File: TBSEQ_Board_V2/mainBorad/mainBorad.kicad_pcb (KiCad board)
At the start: 2 copper layers, 150 x 150 mm, 235 parts, among them IC11 AN6562, IC11_1 AN6562, IC12 4066, IC15 CA3080A, J13 Conn_01x01_Pin, J3 Conn_01x02_Pin, J4 Conn_01x02_Pin, J7 Conn_01x03_Pin, J8 Conn_01x02_Pin, J9 Conn_01x01_Pin, Q10 PNP, Q11 NPN, Q12 HN1C01FU-GR,LF_6P DIP, Q13 NPN, Q14 NPN, Q15 NPN, Q16 NPN, Q17 NPN, Q18 NPN, Q19 NPN, Q20 NPN, Q21 HN1C01FU-GR,LF_6P DIP, Q22 HN1C01FU-GR,LF_6P DIP, Q23 NPN, Q24 NPN, Q25 NPN, Q26 HN1C01FU-GR,LF_6P DIP, Q27 PNP, Q28 NJFET, Q29 NPN, Q30 NPN, Q31 PNP, Q32 NPN, Q35 NPN, Q36 PNP, Q37 NPN, Q38 PNP, Q39 NJFET, Q40 NPN, Q41 NPN, Q8 PNP, Q9 PNP

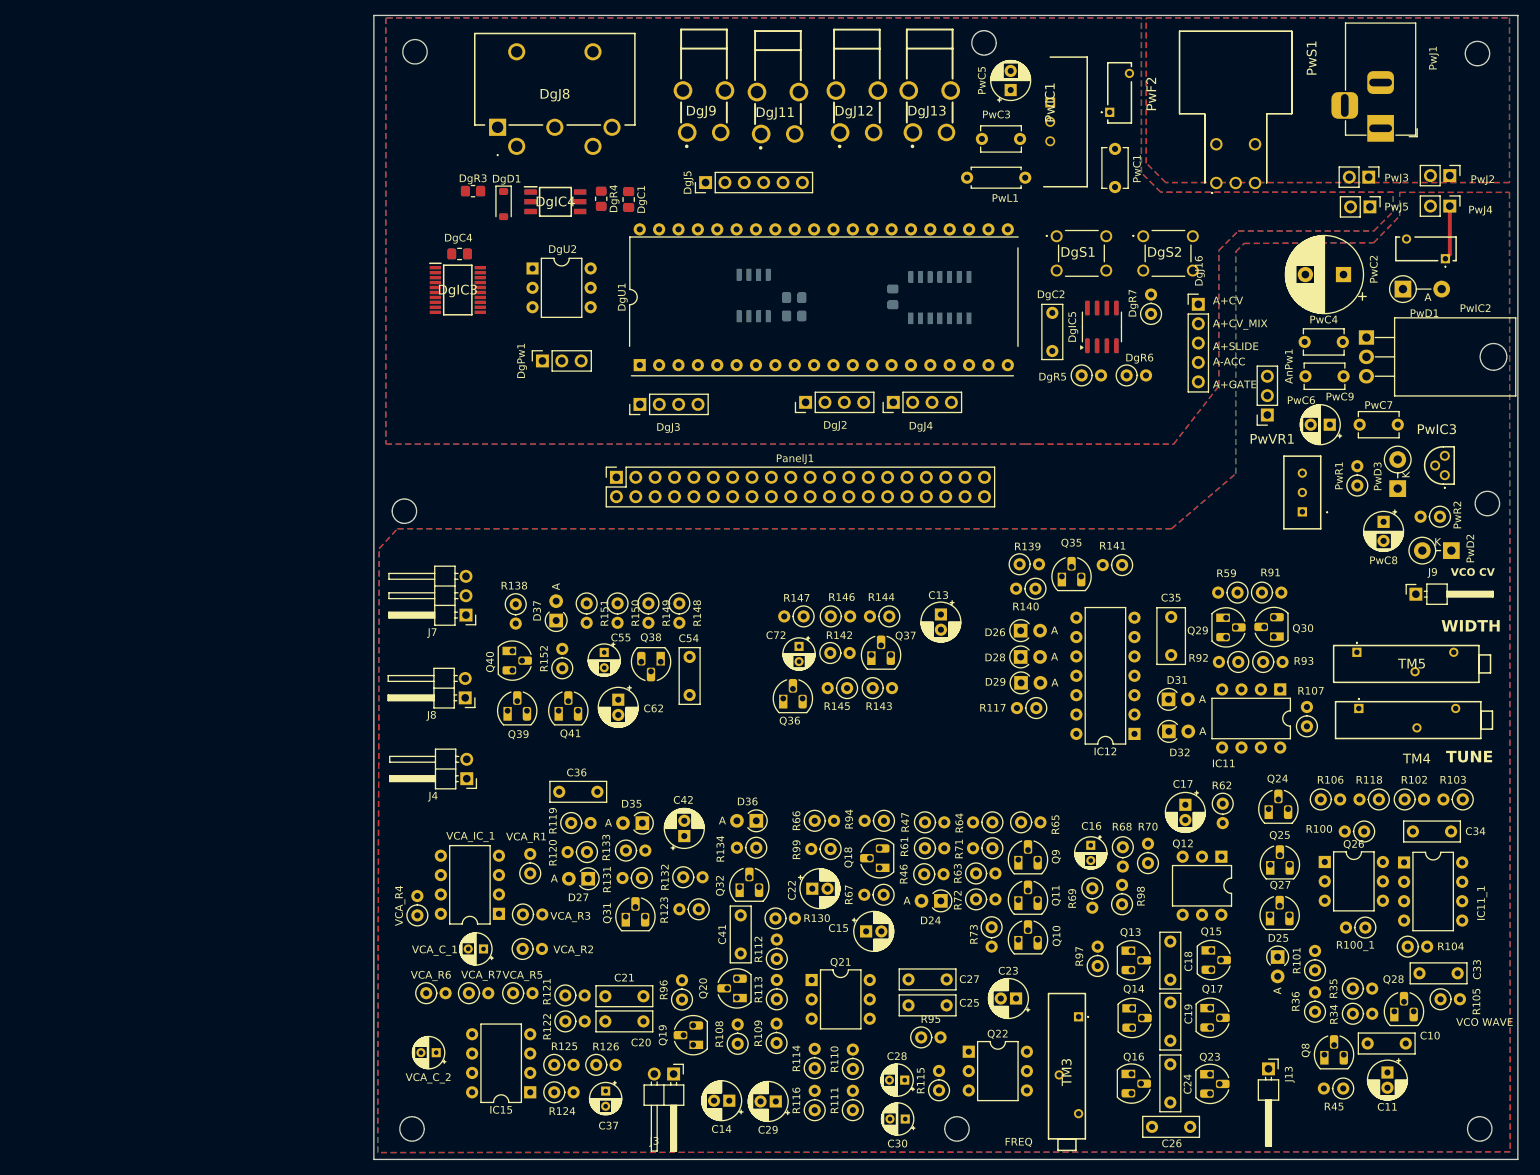
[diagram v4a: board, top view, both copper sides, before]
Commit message: mainborad
DRCチェック通過
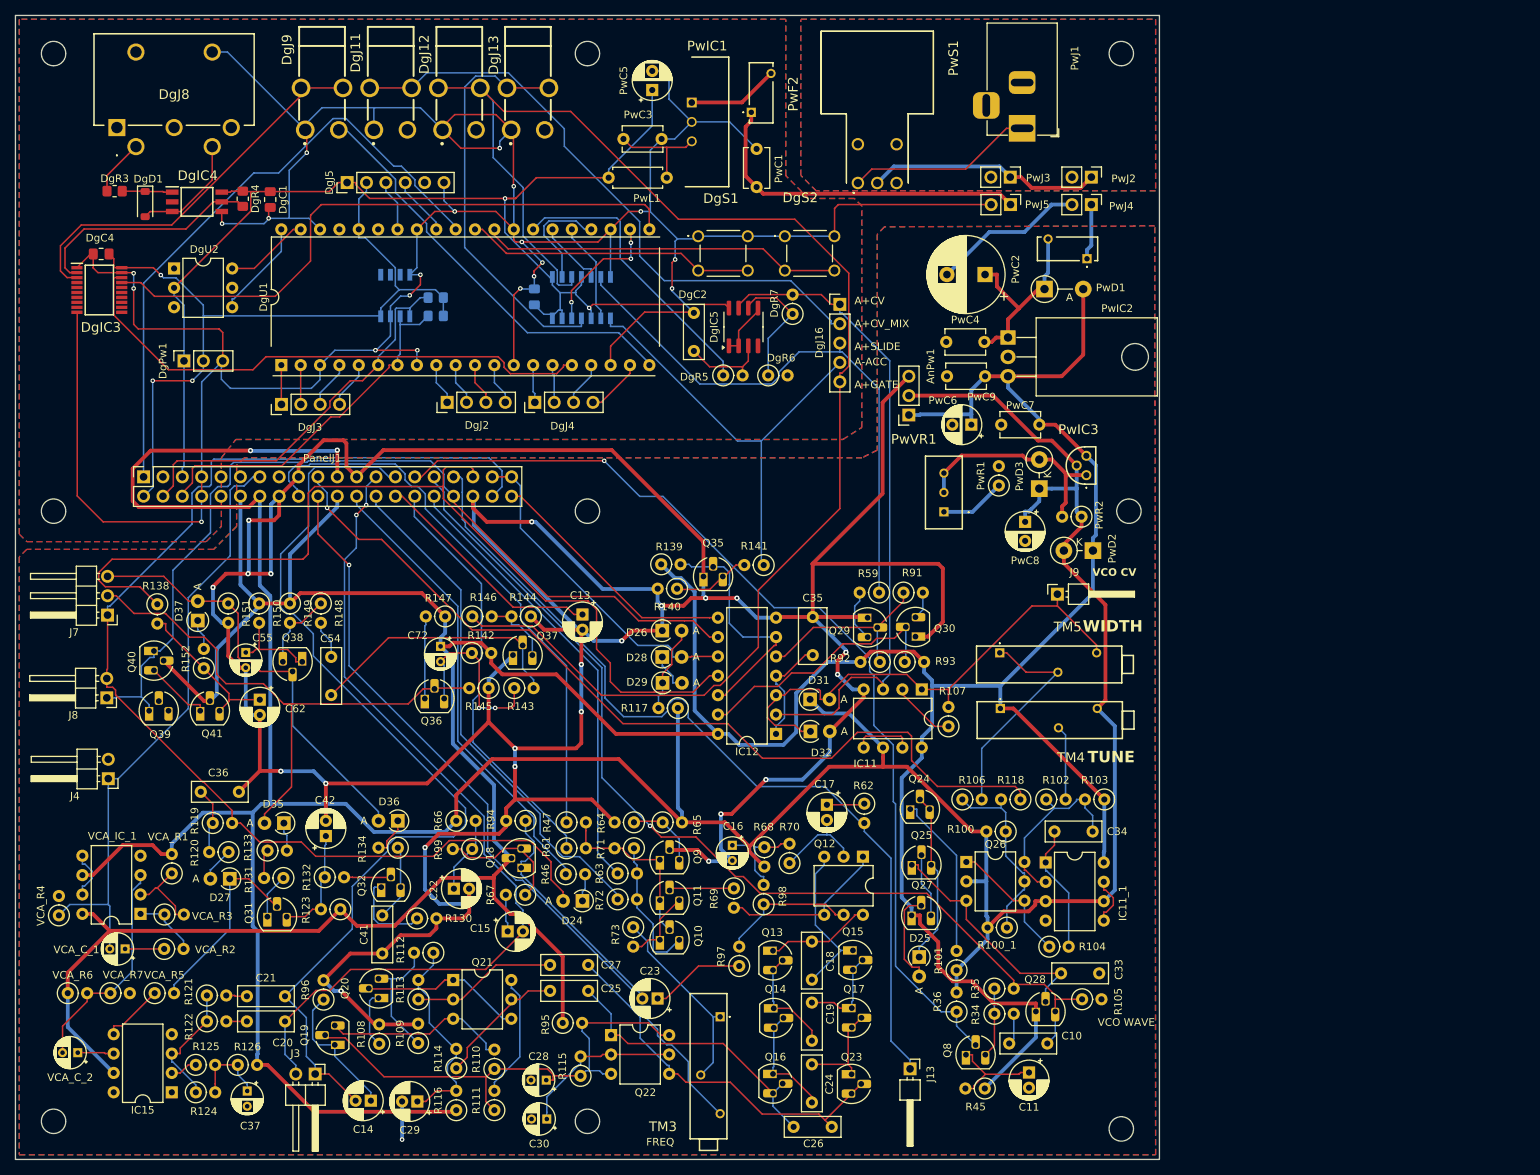
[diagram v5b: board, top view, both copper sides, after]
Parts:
- moved PanelJ1 62.0 mm to (36.8, 80.5)
- moved DgJ13 52.7 mm to (87.2, 24.0)
- moved DgJ12 52.1 mm to (78.2, 24.0)
- moved DgJ11 50.8 mm to (69.2, 24.0)
- moved DgJ9 50.1 mm to (60.2, 24.0)
- moved DgJ8 49.9 mm to (33.3, 34.7)
- moved PwJ5 47.1 mm to (150.5, 44.8)
- moved C25 47.0 mm to (95.1, 147.9)
- moved C27 47.0 mm to (95.1, 144.5)
- moved R115 47.0 mm to (94.1, 159.0)
- moved R95 47.0 mm to (91.8, 152.1)
- moved PwJ2 47.0 mm to (161.1, 41.2)
- moved PwJ4 47.0 mm to (161.1, 44.8)
- moved PwC6 47.0 mm to (145.3, 73.7)
- moved PwC5 47.0 mm to (103.5, 29.8)
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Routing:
- net GNDA: track 0.00 -> 567.8 mm, vias 0 -> 23
- net A+12V: track 0.00 -> 533.7 mm
- net A+5.333V: track 0.00 -> 475.0 mm, vias 0 -> 2
- net GNDD: track 0.00 -> 434.4 mm, vias 0 -> 20
- net A+GATE: track 0.00 -> 195.3 mm
- net D+5V: track 0.00 -> 162.4 mm, vias 0 -> 2
- net A+VCA-Reso_ACC: track 0.00 -> 155.7 mm
- net A+VCO_SAW: track 0.00 -> 131.0 mm, vias 0 -> 1
- net A+VCO_SQU: track 0.00 -> 128.9 mm, vias 0 -> 1
- net A_VR6_CCW: track 0.00 -> 125.9 mm
- net A+VCA_Signal: track 0.00 -> 125.6 mm
- net A+ENV.MOD: track 0.00 -> 118.7 mm
- net A_VR2_WIPER: track 0.00 -> 116.6 mm, vias 0 -> 1
- net A+VCO_WAVE: track 0.00 -> 116.6 mm
- net A+VCA_Resonance: track 0.00 -> 115.4 mm, vias 0 -> 2
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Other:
- outline, holes or cut-outs redrawn

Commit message: mainboard & frontPanel
コメント記入&寸法合わせ
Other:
- outline, holes or cut-outs redrawn
- board text added: "1:VCO_CV"
- board text added: "1:VCO_Wave"
- board text added: "2:GNDA 1:LineOut"
- board text added: "2:VCA_ResoAcc 1:Env.Mod"
- board text added: "2:VCA_Resonance 1:VCA_Signal"
- board text added: "3:GNDA 2:A+5.333V 1:A+12V"
- board text added: "3:VCA_Env 2:VCA_Trig 1:VCA_ResoAcc"
- board text added: "CV Out"
- board text added: "D+3.3V"
- board text added: "D+5V"
- board text added: "DC+15V"
- board text added: "GNDD"
- board text added: "Gate Out"
- board text added: "MIDI In"
- board text added: "PowerSW"
- board text added: "ResetButton"
- board text added: "Sync In"
- board text added: "Sync Out"
- board text added: "TB-SEQ Ver2 mainBoard 2024/10/14"
- board text added: "TestButton"
- board text removed: "VCO CV"
- board text removed: "VCO WAVE"

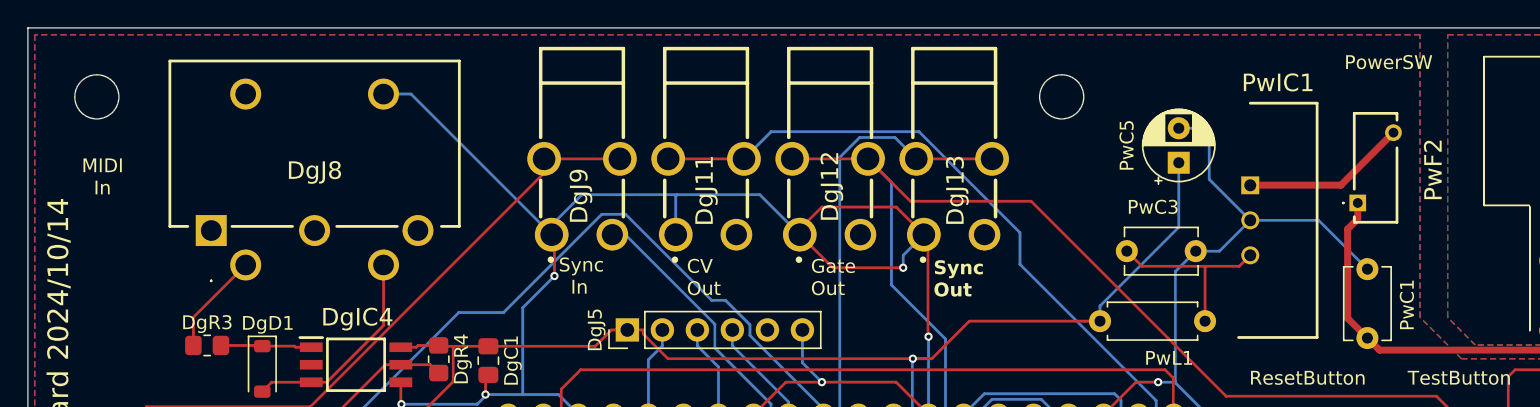
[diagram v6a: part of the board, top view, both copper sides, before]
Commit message: mainBoard&FrontPanel
微修正
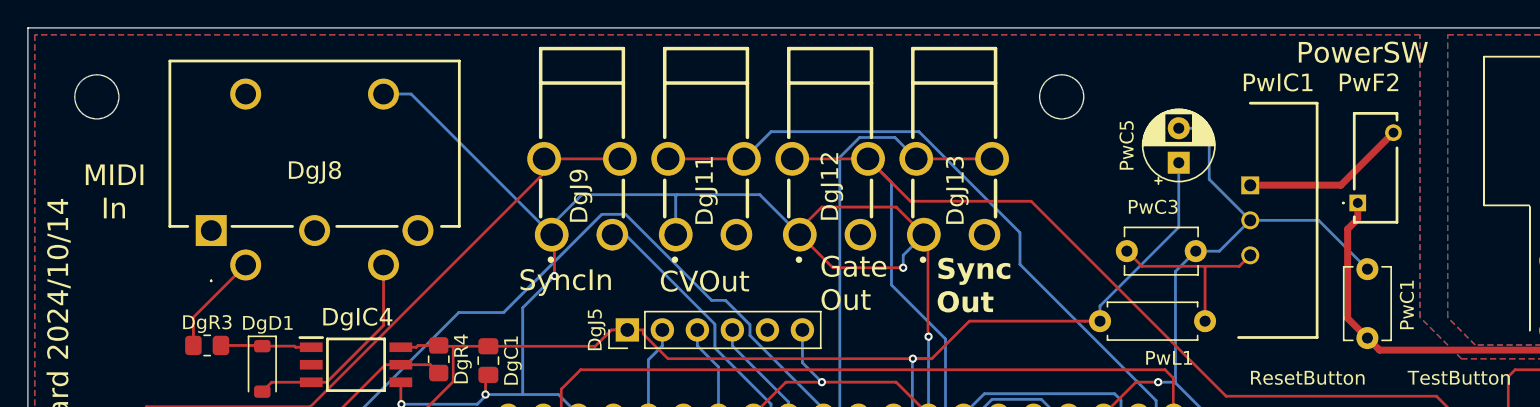
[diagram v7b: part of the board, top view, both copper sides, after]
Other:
- board text added: "CVOut"
- board text added: "SyncIn"
- board text removed: "CV Out"
- board text removed: "Sync In"
